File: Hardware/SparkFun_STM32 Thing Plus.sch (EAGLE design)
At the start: 66 parts, among them J3 QWIIC_RA, J6 CORTEX_DEBUG, J7 MICRO-SD, U1 MCP73831, U2 3.3V, U3 W25QXX128MBIT-6X5, U4 STM32F405RGT6, Y1 32.768kHz, Y2 12MHz

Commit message: Updated V01
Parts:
- added LOGO3: OSHW-LOGOS, SparkFun-Aesthetics:OSHW-LOGOS
- C16, C17: value 22pF -> 15pF; device SparkFun-Capacitors:22PF-0402T-16V-10% -> SparkFun-Capacitors:15PF-0402T-50V-5%
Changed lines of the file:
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@@
 <part name="Y1" library="SparkFun-Clocks" deviceset="CRYSTAL-32.768KHZ" device="SMD-3.2X1.5" value="32.768kHz"/>
 <part name="Y2" library="SparkFun-Clocks" deviceset="CRYSTAL-12MHZ" device="&quot;" value="12MHz"/>
-<part name="C16" library="SparkFun-Capacitors" deviceset="22PF" device="-0402T-16V-10%" value="22pF"/>
-<part name="C17" library="SparkFun-Capacitors" deviceset="22PF" device="-0402T-16V-10%" value="22pF"/>
+<part name="C16" library="SparkFun-Capacitors" deviceset="15PF" device="-0402T-50V-5%" value="15pF"/>
+<part name="C17" library="SparkFun-Capacitors" deviceset="15PF" device="-0402T-50V-5%" value="15pF"/>
 <part name="C18" library="SparkFun-Capacitors" deviceset="22PF" device="-0402T-16V-10%" value="22pF"/>
 <part name="C19" library="SparkFun-Capacitors" deviceset="22PF" device="-0402T-16V-10%" value="22pF"/>
@@
 <part name="GND38" library="SparkFun-PowerSymbols" deviceset="GND" device=""/>
 <part name="SUPPLY26" library="SparkFun-PowerSymbols" deviceset="3.3V" device=""/>
+<part name="LOGO3" library="SparkFun-Aesthetics" deviceset="OSHW-LOGO" device="S"/>
 </parts>
 <sheets>
@@
 <attribute name="VALUE" x="71.12" y="109.22" size="1.778" layer="96" font="vector" rot="R90" align="top-left"/>
 </instance>
-<instance part="LOGO1" gate="G$1" x="160.02" y="40.64" smashed="yes"/>
-<instance part="LOGO2" gate="G$1" x="175.26" y="35.56" smashed="yes"/>
+<instance part="LOGO1" gate="G$1" x="157.48" y="40.64" smashed="yes"/>
+<instance part="LOGO2" gate="G$1" x="167.64" y="35.56" smashed="yes"/>
 <instance part="SUPPLY25" gate="G$1" x="137.16" y="177.8" smashed="yes">
 <attribute name="VALUE" x="137.16" y="180.594" size="1.778" layer="96" font="vector" align="bottom-center"/>
@@
 <attribute name="VALUE" x="170.18" y="178.054" size="1.778" layer="96" font="vector" align="bottom-center"/>
 </instance>
+<instance part="LOGO3" gate="G$1" x="236.22" y="45.72" smashed="yes"/>
 </instances>
 <busses>

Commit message: Updated version number to V10
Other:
- note added: "v10"
- note removed: "v01"
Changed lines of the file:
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@@
 <sheet>
 <plain>
-<text x="238.76" y="7.62" size="2.54" layer="94" font="vector">v01</text>
+<text x="238.76" y="7.62" size="2.54" layer="94" font="vector">v10</text>
 <text x="165.608" y="11.176" size="2.54" layer="94" font="vector">Alex Wende</text>
 <text x="2.54" y="124.46" size="2.54" layer="94" font="vector" ratio="15">3.3V Regulator</text>

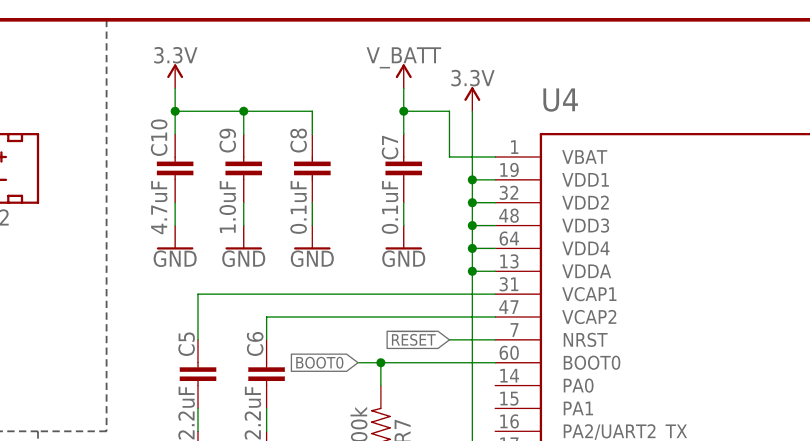
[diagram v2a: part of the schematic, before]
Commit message: V10 design review changes
Replaced V_BAT pin connection on STM32 to test point
Moved microSD connector to center card on PCB instead of footprint
Removed overlapping labels on bottom
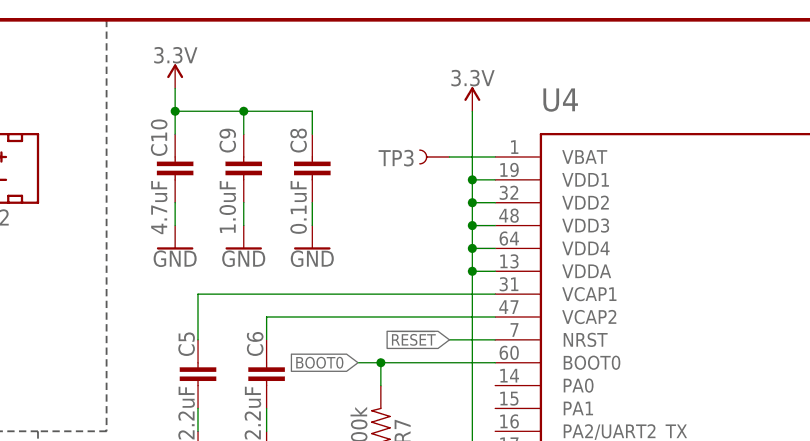
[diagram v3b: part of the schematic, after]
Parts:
- removed C7: 0.1uF, SparkFun-Capacitors:0.1UF-0402T-10V-10%-X7R
- added TP3: TEST-POINT3, SparkFun-Connectors:TEST-POINT3
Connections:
- new net N$4: TP3.1, U4.VBAT
- net GND: no longer C7.2
- net V_BATT: no longer C7.1, U4.VBAT
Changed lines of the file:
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@@
 <part name="GND2" library="SparkFun-PowerSymbols" deviceset="GND" device=""/>
 <part name="GND4" library="SparkFun-PowerSymbols" deviceset="GND" device=""/>
-<part name="C7" library="SparkFun-Capacitors" deviceset="0.1UF" device="-0402T-10V-10%-X7R" value="0.1uF"/>
 <part name="C8" library="SparkFun-Capacitors" deviceset="0.1UF" device="-0402T-10V-10%-X7R" value="0.1uF"/>
 <part name="C9" library="SparkFun-Capacitors" deviceset="1.0UF" device="-0402T-16V-10%" value="1.0uF"/>
@@
 <part name="GND5" library="SparkFun-PowerSymbols" deviceset="GND" device=""/>
 <part name="GND7" library="SparkFun-PowerSymbols" deviceset="GND" device=""/>
-<part name="GND8" library="SparkFun-PowerSymbols" deviceset="GND" device=""/>
 <part name="GND9" library="SparkFun-PowerSymbols" deviceset="GND" device=""/>
 <part name="GND12" library="SparkFun-PowerSymbols" deviceset="GND" device=""/>
@@
 <part name="R9" library="SparkFun-Resistors" deviceset="22OHM" device="-0603-1/10W-1%" value="22"/>
 <part name="R10" library="SparkFun-Resistors" deviceset="22OHM" device="-0603-1/10W-1%" value="22"/>
-<part name="SUPPLY7" library="SparkFun-PowerSymbols" deviceset="V_BATT" device=""/>
 <part name="GND36" library="SparkFun-PowerSymbols" deviceset="GND" device=""/>
 <part name="C20" library="SparkFun-Capacitors" deviceset="0.1UF" device="-0402T-10V-10%-X7R" value="0.1uF"/>
@@
 <part name="SUPPLY26" library="SparkFun-PowerSymbols" deviceset="3.3V" device=""/>
 <part name="LOGO3" library="SparkFun-Aesthetics" deviceset="OSHW-LOGO" device="S"/>
+<part name="TP3" library="SparkFun-Connectors" deviceset="TEST-POINT" device="3" value=""/>
 </parts>
 <sheets>
@@
 <attribute name="VALUE" x="147.32" y="136.906" size="1.778" layer="96" font="vector" rot="MR0" align="top-center"/>
 </instance>
-<instance part="C7" gate="G$1" x="162.56" y="167.64" smashed="yes" rot="MR0">
-<attribute name="NAME" x="161.925" y="172.72" size="1.778" layer="95" font="vector" rot="MR270"/>
-<attribute name="VALUE" x="161.925" y="167.64" size="1.778" layer="96" font="vector" rot="MR270"/>
-</instance>
 <instance part="C8" gate="G$1" x="152.4" y="167.64" smashed="yes" rot="MR0">
 <attribute name="NAME" x="151.765" y="173.482" size="1.778" layer="95" font="vector" rot="MR270"/>
@@
 <attribute name="VALUE" x="154.94" y="111.506" size="1.778" layer="96" font="vector" align="top-center"/>
 </instance>
-<instance part="GND8" gate="1" x="162.56" y="160.02" smashed="yes">
-<attribute name="VALUE" x="162.56" y="159.766" size="1.778" layer="96" font="vector" align="top-center"/>
-</instance>
 <instance part="GND9" gate="1" x="137.16" y="160.02" smashed="yes">
 <attribute name="VALUE" x="137.16" y="159.766" size="1.778" layer="96" font="vector" align="top-center"/>
@@
 <attribute name="NAME" x="30.48" y="164.084" size="1.778" layer="95" font="vector" align="bottom-center"/>
 <attribute name="VALUE" x="35.56" y="164.084" size="1.778" layer="96" font="vector" rot="R180" align="top-center"/>
-</instance>
-<instance part="SUPPLY7" gate="G$1" x="162.56" y="177.8" smashed="yes">
-<attribute name="VALUE" x="162.56" y="180.594" size="1.778" layer="96" font="vector" align="bottom-center"/>
 </instance>
 <instance part="GND36" gate="1" x="63.5" y="5.08" smashed="yes" rot="MR0">
@@
 </instance>
 <instance part="LOGO3" gate="G$1" x="236.22" y="45.72" smashed="yes"/>
+<instance part="TP3" gate="G$1" x="167.64" y="170.18" smashed="yes" rot="R180">
+<attribute name="NAME" x="163.83" y="170.942" size="1.778" layer="95" font="vector" rot="R180"/>
+<attribute name="VALUE" x="170.18" y="172.72" size="1.778" layer="96" font="vector" rot="R180"/>
+</instance>
 </instances>
 <busses>
@@
 <pinref part="GND7" gate="1" pin="GND"/>
 <wire x1="154.94" y1="116.84" x2="154.94" y2="114.3" width="0.1524" layer="91"/>
-</segment>
-<segment>
-<pinref part="C7" gate="G$1" pin="2"/>
-<wire x1="162.56" y1="165.1" x2="162.56" y2="162.56" width="0.1524" layer="91"/>
-<pinref part="GND8" gate="1" pin="GND"/>
 </segment>
 <segment>
@@
 </segment>
 <segment>
-<pinref part="U4" gate="G$1" pin="VBAT"/>
-<wire x1="172.72" y1="170.18" x2="167.64" y2="170.18" width="0.1524" layer="91"/>
-<wire x1="167.64" y1="170.18" x2="167.64" y2="175.26" width="0.1524" layer="91"/>
-<wire x1="167.64" y1="175.26" x2="162.56" y2="175.26" width="0.1524" layer="91"/>
-<pinref part="C7" gate="G$1" pin="1"/>
-<wire x1="162.56" y1="172.72" x2="162.56" y2="175.26" width="0.1524" layer="91"/>
-<pinref part="SUPPLY7" gate="G$1" pin="V_BATT"/>
-<wire x1="162.56" y1="177.8" x2="162.56" y2="175.26" width="0.1524" layer="91"/>
-<junction x="162.56" y="175.26"/>
-</segment>
-<segment>
 <pinref part="J4" gate="G$1" pin="12"/>
 <wire x1="45.72" y1="58.42" x2="43.18" y2="58.42" width="0.1524" layer="91"/>
@@
 </segment>
 </net>
+<net name="N$4" class="0">
+<segment>
+<pinref part="U4" gate="G$1" pin="VBAT"/>
+<wire x1="172.72" y1="170.18" x2="167.64" y2="170.18" width="0.1524" layer="91"/>
+<pinref part="TP3" gate="G$1" pin="1"/>
+</segment>
+</net>

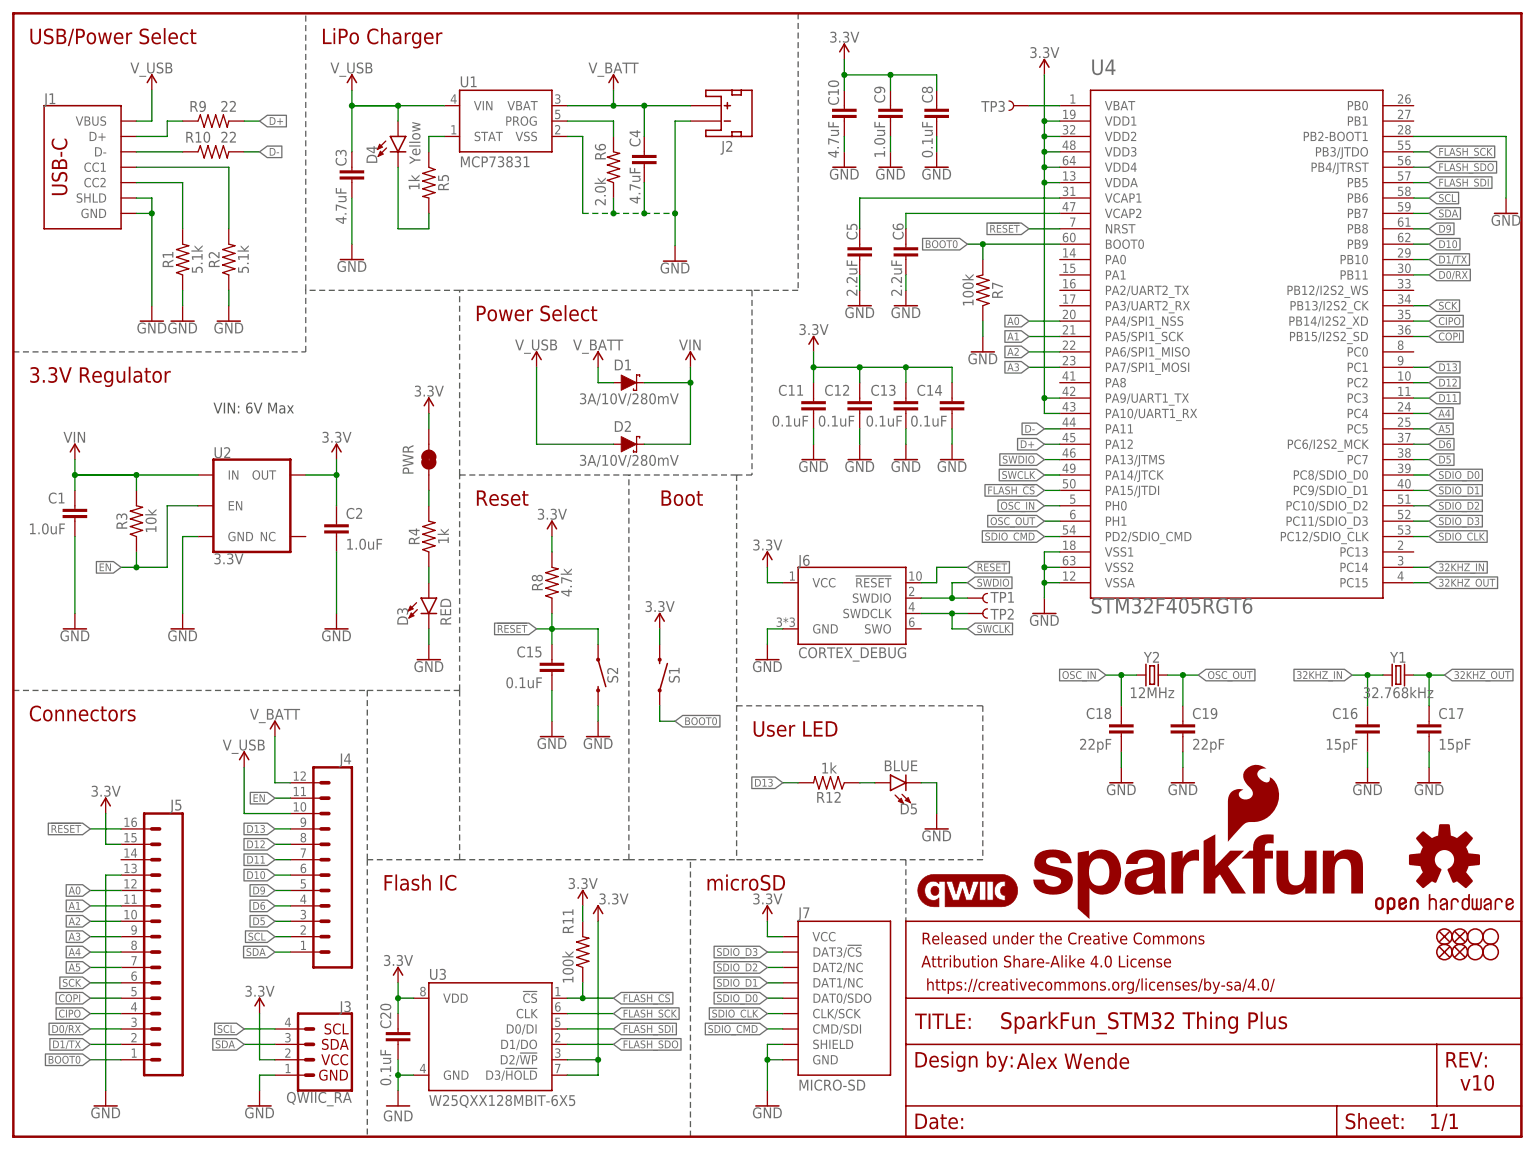
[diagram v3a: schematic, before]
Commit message: Double-check changes
Schematic
- Added VDD range
- Added RTC Battery range

Board
- Updated labels
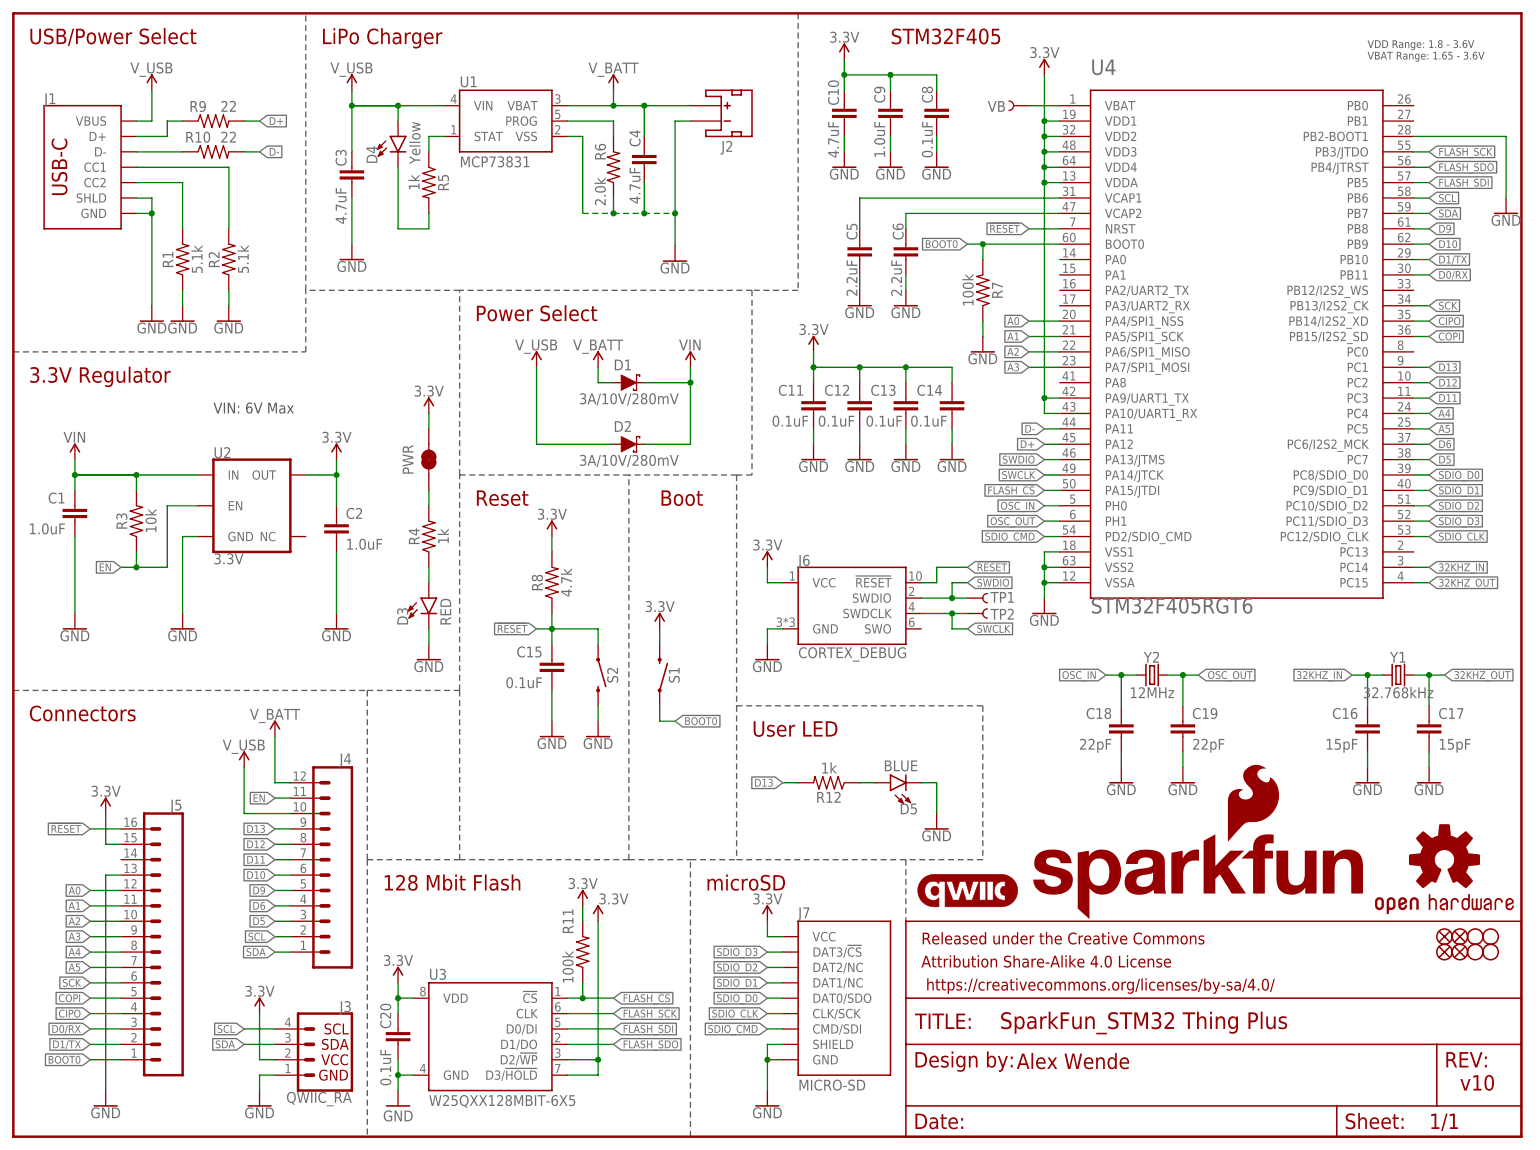
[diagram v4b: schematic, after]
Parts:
- renumbered TP3 to VB
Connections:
- net N$4 renamed VB
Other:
- note added: "128 Mbit Flash"
- note added: "STM32F405"
- note added: "VDD Range: 1.8 - 3.6V VBAT Range: 1.65 - 3.6V"
- note removed: "Flash IC"
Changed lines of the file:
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@@
 <part name="SUPPLY26" library="SparkFun-PowerSymbols" deviceset="3.3V" device=""/>
 <part name="LOGO3" library="SparkFun-Aesthetics" deviceset="OSHW-LOGO" device="S"/>
-<part name="TP3" library="SparkFun-Connectors" deviceset="TEST-POINT" device="3" value=""/>
+<part name="VB" library="SparkFun-Connectors" deviceset="TEST-POINT" device="3" value=""/>
 </parts>
 <sheets>
@@
 <text x="2.54" y="68.58" size="2.54" layer="94" font="vector" ratio="15">Connectors</text>
 <text x="114.3" y="40.64" size="2.54" layer="94" font="vector" ratio="15">microSD</text>
-<text x="60.96" y="40.64" size="2.54" layer="94" font="vector" ratio="15">Flash IC</text>
+<text x="60.96" y="40.64" size="2.54" layer="94" font="vector" ratio="15">128 Mbit Flash</text>
 <wire x1="111.76" y1="0" x2="111.76" y2="45.72" width="0.2032" layer="97" style="longdash"/>
 <wire x1="73.66" y1="45.72" x2="58.42" y2="45.72" width="0.2032" layer="97" style="longdash"/>
@@
 <wire x1="160.02" y1="71.12" x2="160.02" y2="45.72" width="0.2032" layer="97" style="longdash"/>
 <wire x1="160.02" y1="45.72" x2="147.32" y2="45.72" width="0.2032" layer="97" style="longdash"/>
+<text x="223.52" y="177.8" size="1.27" layer="97">VDD Range: 1.8 - 3.6V
+VBAT Range: 1.65 - 3.6V</text>
+<text x="144.78" y="180.34" size="2.54" layer="94" font="vector" ratio="15">STM32F405</text>
 </plain>
 <instances>
@@
 </instance>
 <instance part="LOGO3" gate="G$1" x="236.22" y="45.72" smashed="yes"/>
-<instance part="TP3" gate="G$1" x="167.64" y="170.18" smashed="yes" rot="R180">
+<instance part="VB" gate="G$1" x="167.64" y="170.18" smashed="yes" rot="R180">
 <attribute name="NAME" x="163.83" y="170.942" size="1.778" layer="95" font="vector" rot="R180"/>
 <attribute name="VALUE" x="170.18" y="172.72" size="1.778" layer="96" font="vector" rot="R180"/>
@@
 </segment>
 </net>
-<net name="N$4" class="0">
+<net name="VB" class="0">
 <segment>
 <pinref part="U4" gate="G$1" pin="VBAT"/>
 <wire x1="172.72" y1="170.18" x2="167.64" y2="170.18" width="0.1524" layer="91"/>
-<pinref part="TP3" gate="G$1" pin="1"/>
+<pinref part="VB" gate="G$1" pin="1"/>
 </segment>
 </net>
@@
 </drawing>
 <compatibility>
+<note version="6.3" minversion="6.2.2" severity="warning">
+Since Version 6.2.2 text objects can contain more than one line,
+which will not be processed correctly with this version.
+</note>
 <note version="8.3" severity="warning">
 Since Version 8.3, EAGLE supports URNs for individual library

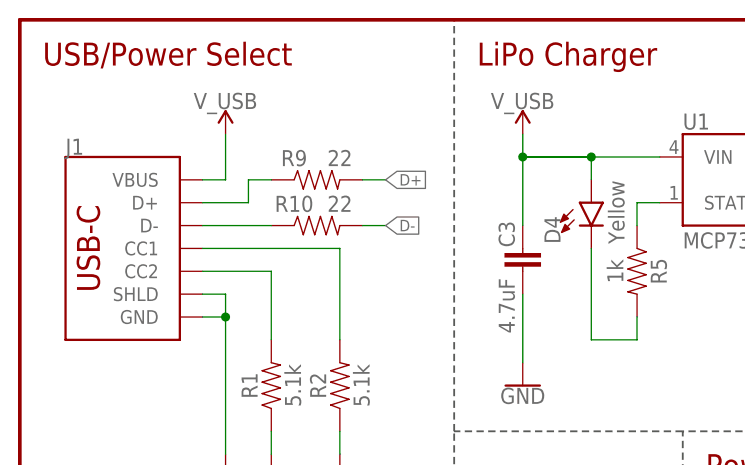
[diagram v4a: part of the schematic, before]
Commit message: BOM update
Replaced 22 ohm resistors with 0 ohm
Replaced old momentary switches to taller momentary switches
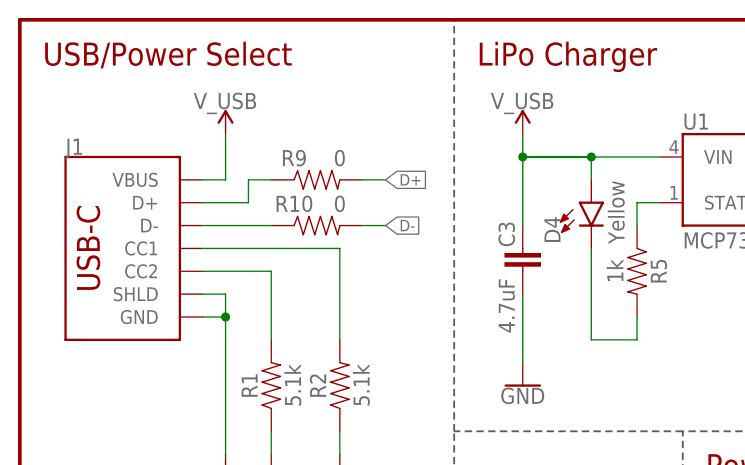
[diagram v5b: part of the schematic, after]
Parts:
- R10, R9: value 22 -> 0; device SparkFun-Resistors:22OHM-0603-1/10W-1% -> SparkFun-Resistors:0OHM-0603-1/10W
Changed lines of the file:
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@@
 <?xml version="1.0" encoding="utf-8"?>
 <!DOCTYPE eagle SYSTEM "eagle.dtd">
-<eagle version="9.6.2">
+<eagle version="9.5.2">
 <drawing>
 <settings>
@@
 <part name="GND28" library="SparkFun-PowerSymbols" deviceset="GND" device=""/>
 <part name="SUPPLY6" library="SparkFun-PowerSymbols" deviceset="V_USB" device=""/>
-<part name="R9" library="SparkFun-Resistors" deviceset="22OHM" device="-0603-1/10W-1%" value="22"/>
-<part name="R10" library="SparkFun-Resistors" deviceset="22OHM" device="-0603-1/10W-1%" value="22"/>
+<part name="R9" library="SparkFun-Resistors" deviceset="0OHM" device="-0603-1/10W" value="0"/>
+<part name="R10" library="SparkFun-Resistors" deviceset="0OHM" device="-0603-1/10W" value="0"/>
 <part name="GND36" library="SparkFun-PowerSymbols" deviceset="GND" device=""/>
 <part name="C20" library="SparkFun-Capacitors" deviceset="0.1UF" device="-0402T-10V-10%-X7R" value="0.1uF"/>
